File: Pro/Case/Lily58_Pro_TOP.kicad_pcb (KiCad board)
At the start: 2 copper layers, 142.5 x 106.3 mm, 5 parts

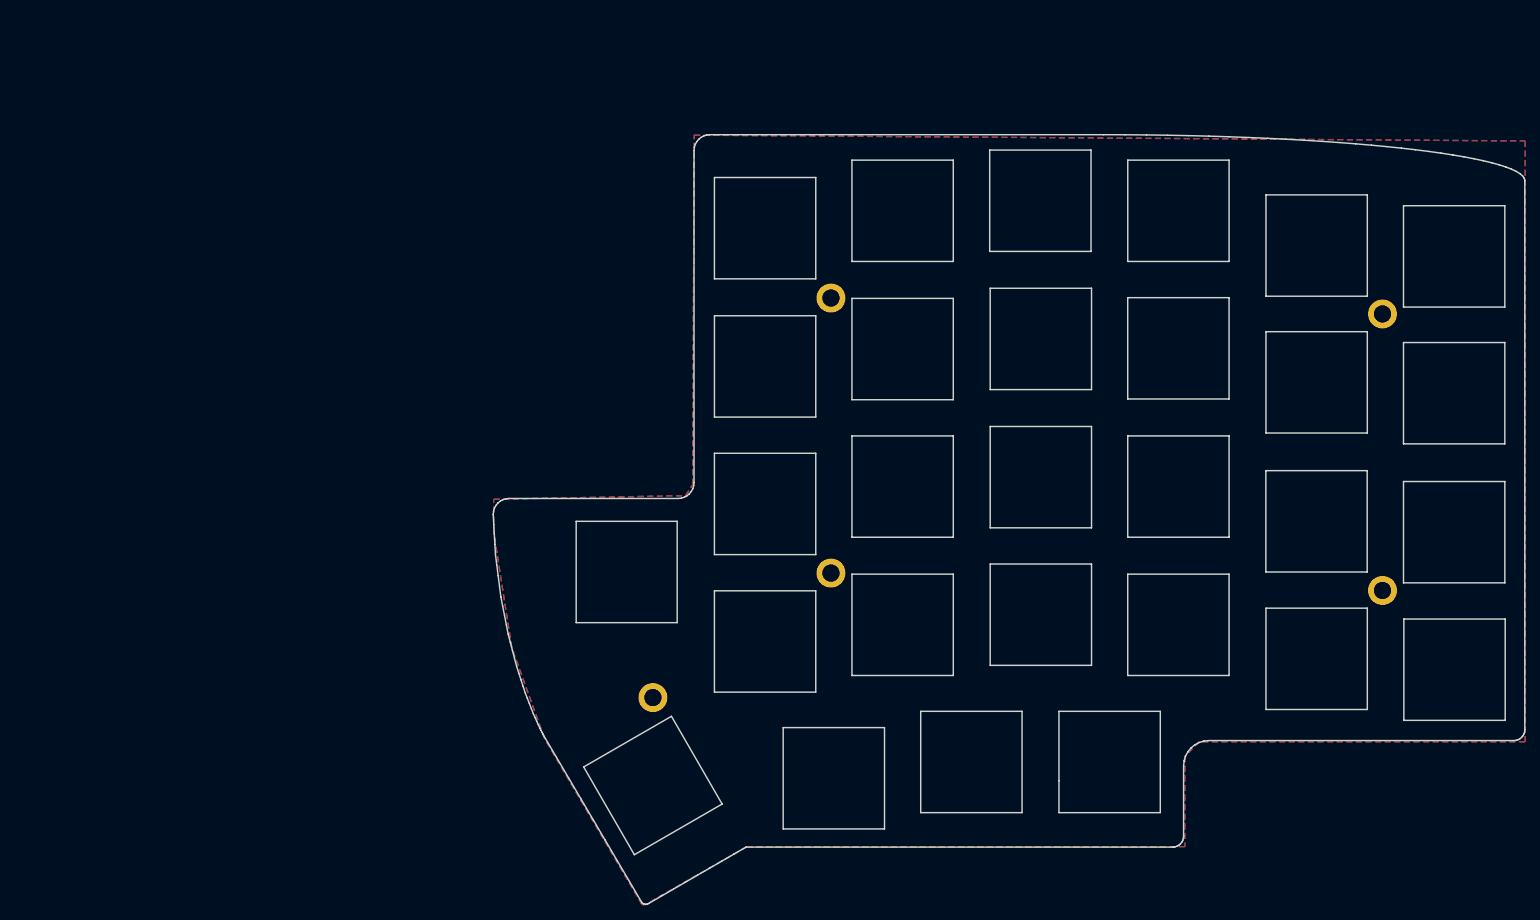
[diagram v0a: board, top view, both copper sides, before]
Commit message: Close open edges to allow 3D render and import to FreeCAD
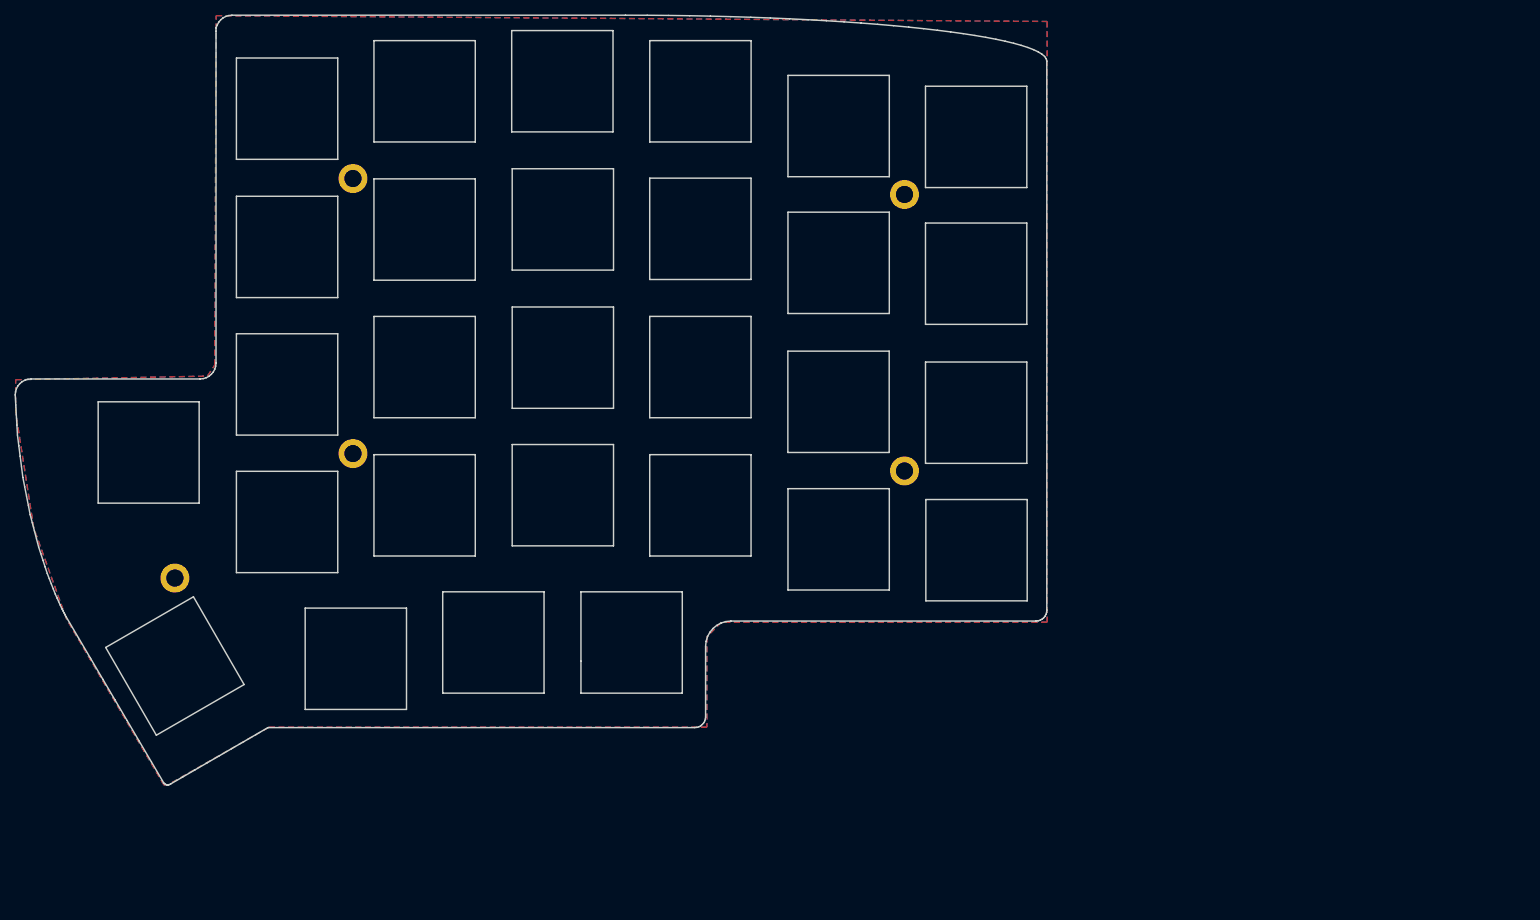
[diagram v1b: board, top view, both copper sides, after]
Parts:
- moved Hol4 68.1 mm to (139.8, 43.4)
- moved Hol5 68.1 mm to (139.8, 81.6)
- moved Hol1 68.1 mm to (63.6, 79.2)
- moved Hol2 68.1 mm to (39.0, 96.4)
- moved Hol3 68.1 mm to (63.6, 41.2)
- renumbered REF** to Hol1, REF** to Hol2, REF** to Hol3, REF** to Hol4, REF** to Hol5
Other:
- outline, holes or cut-outs redrawn
